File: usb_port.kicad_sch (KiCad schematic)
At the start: 14 parts, among them J1 USB_C_Receptacle, U12 MT9700

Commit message: Finish layout
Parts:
- renumbered C76 to C68, C66 to C78, C67 to C79, C69 to C81, D9 to D12, F12 to F15, FB17 to FB23, FB18 to FB24, U12 to U15

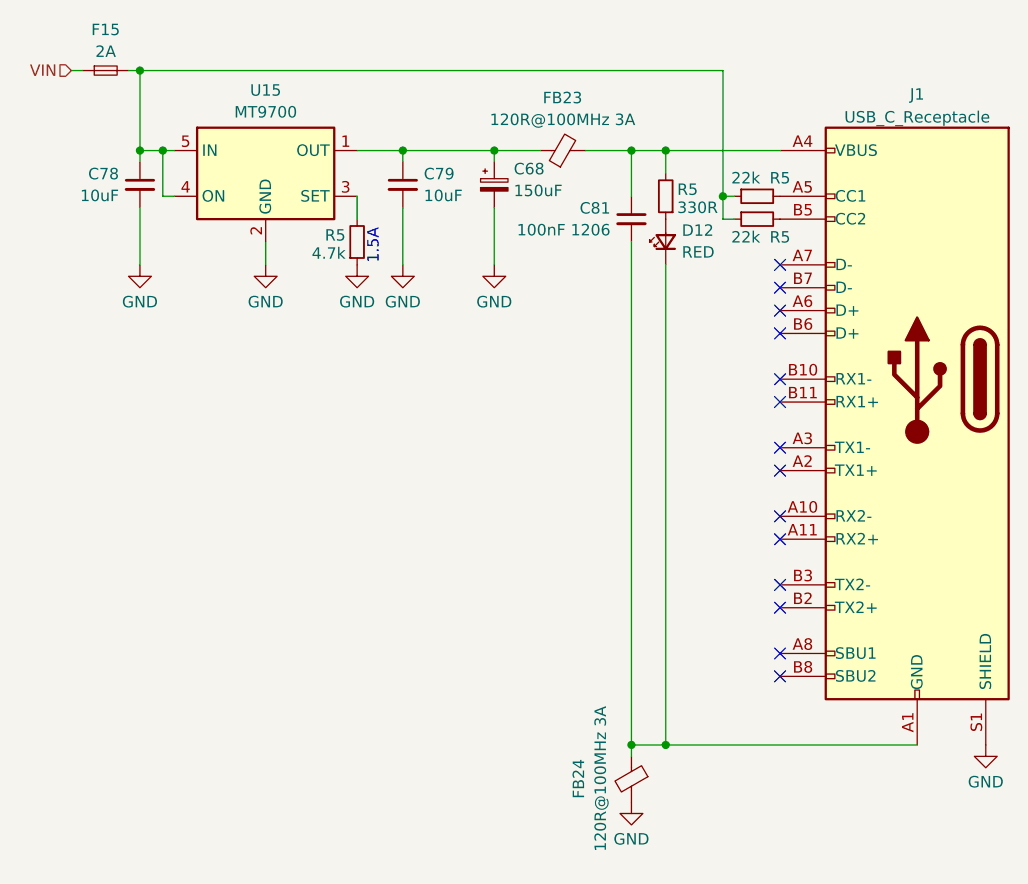
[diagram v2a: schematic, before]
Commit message: Supply regulator enable from CYPD LDO
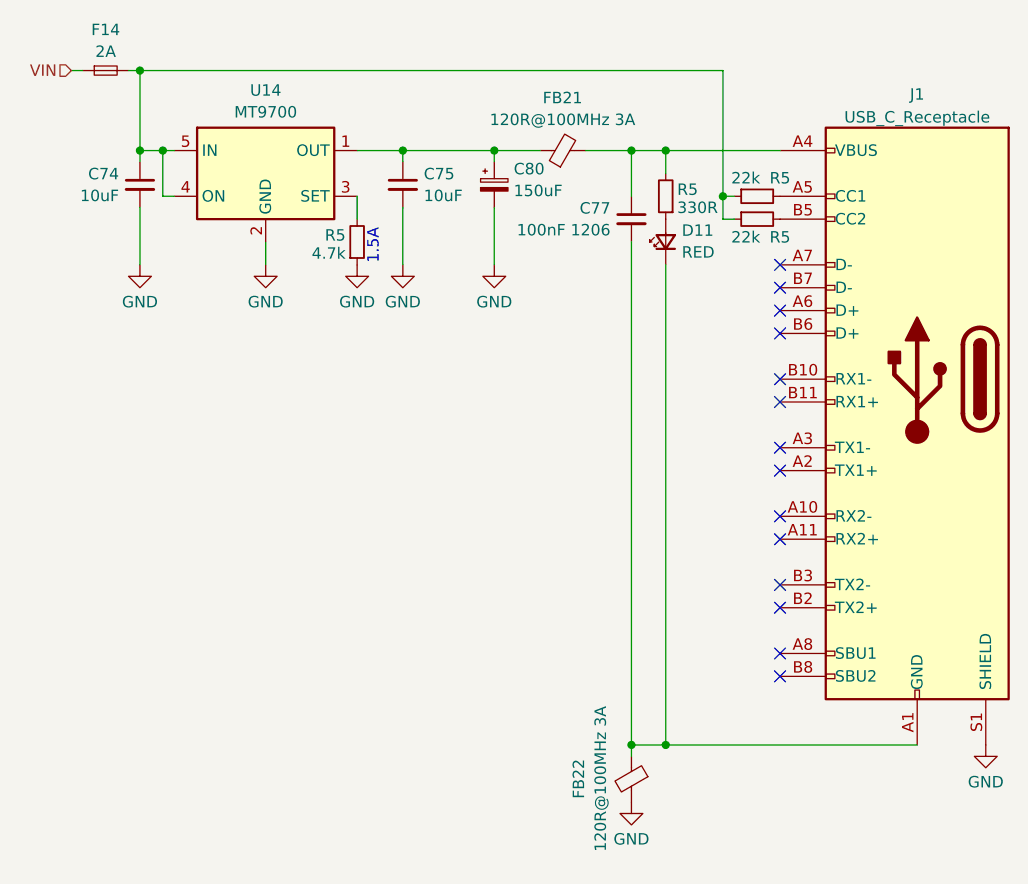
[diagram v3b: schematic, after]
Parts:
- renumbered C78 to C74, C79 to C75, C81 to C77, C68 to C80, D12 to D11, F15 to F14, FB23 to FB21, FB24 to FB22, U15 to U14

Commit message: Consolidate bom items
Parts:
- C74, C75: LCSC C15850 -> C440198

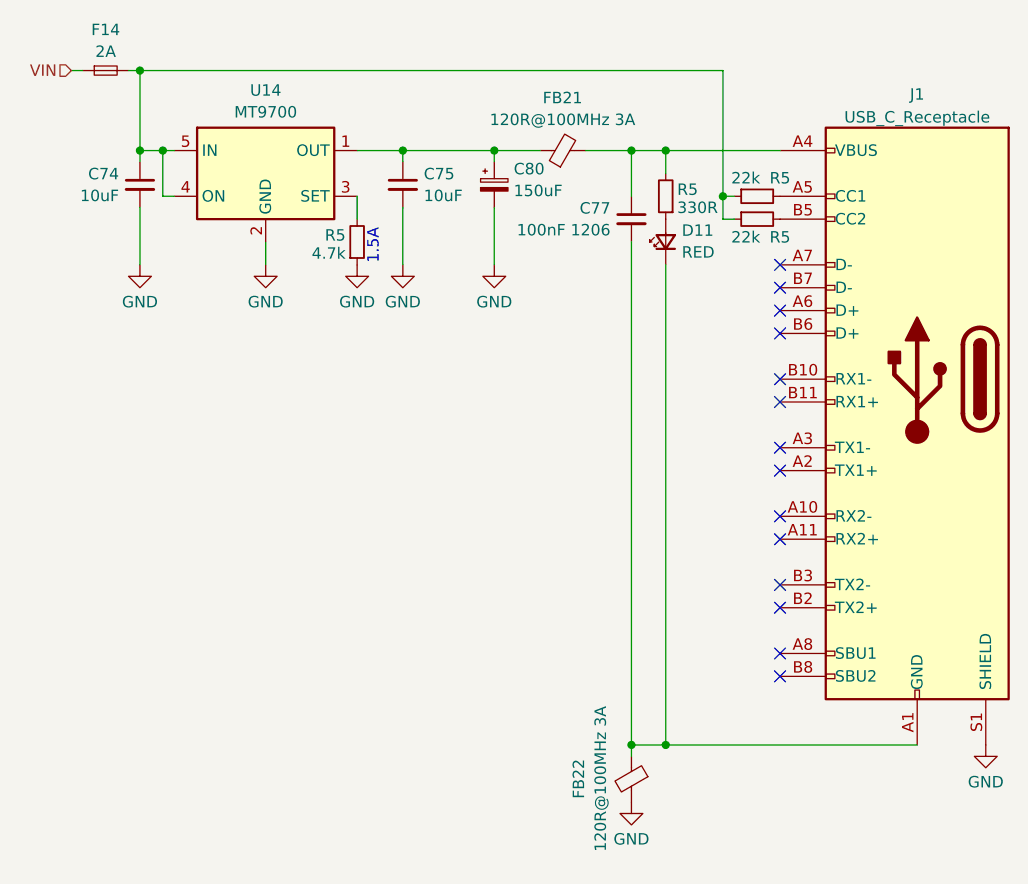
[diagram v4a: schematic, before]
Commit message: Fix LED partnumber
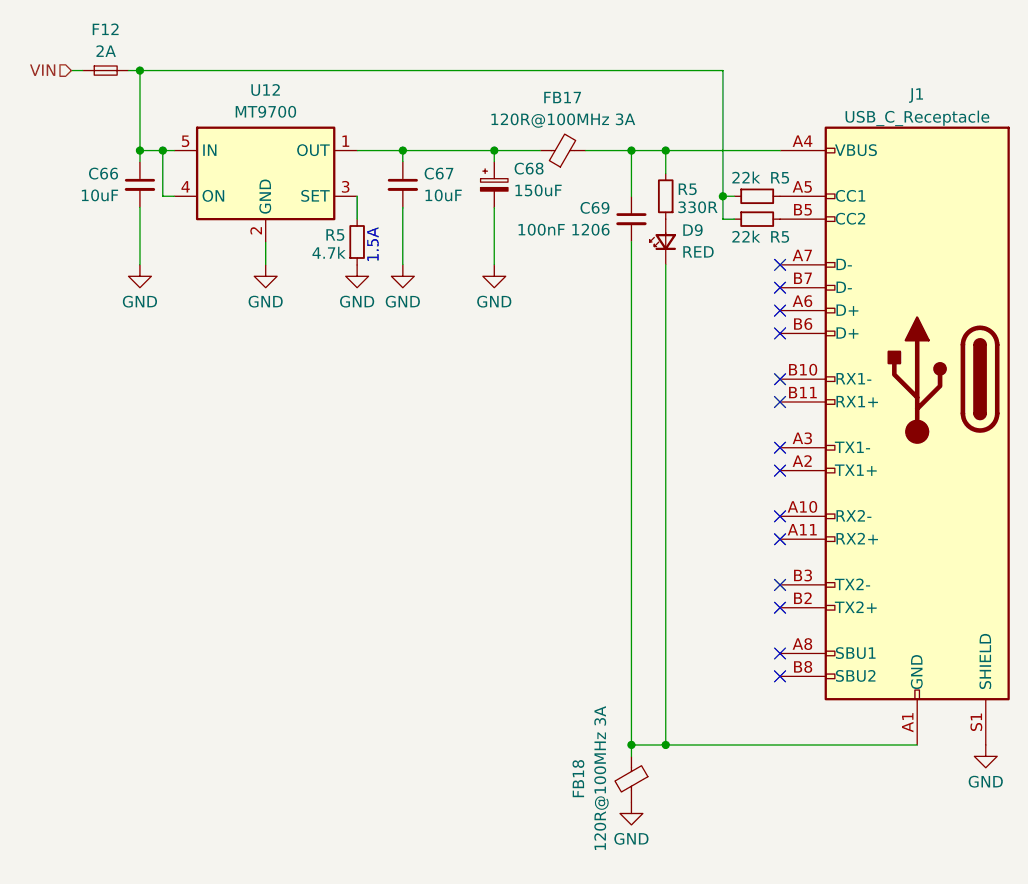
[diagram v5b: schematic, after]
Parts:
- D9: renamed from D11; LCSC C25900 -> C99771
- renumbered C74 to C66, C75 to C67, C80 to C68, C77 to C69, F14 to F12, FB21 to FB17, FB22 to FB18, U14 to U12

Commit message: Add TVS to port groups
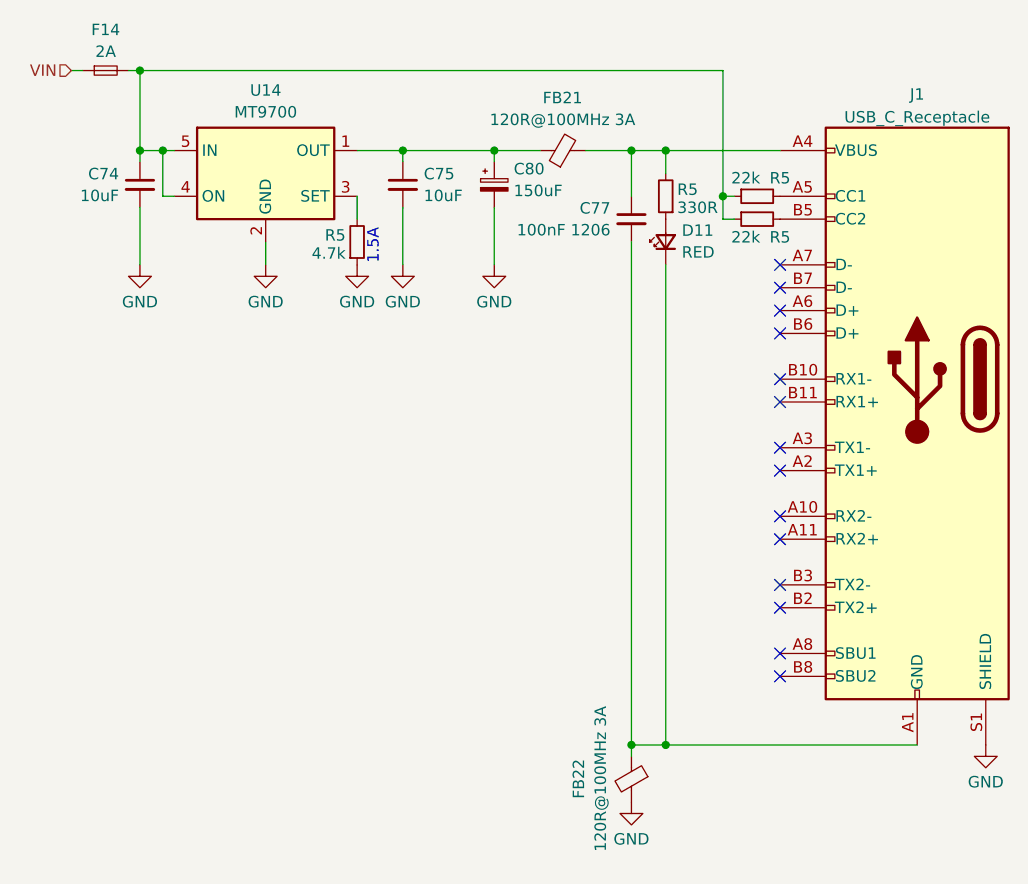
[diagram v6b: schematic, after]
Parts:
- renumbered C66 to C74, C67 to C75, C69 to C77, C68 to C80, D9 to D11, F12 to F14, FB17 to FB21, FB18 to FB22, U12 to U14

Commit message: Advertise all charging ports as DCP
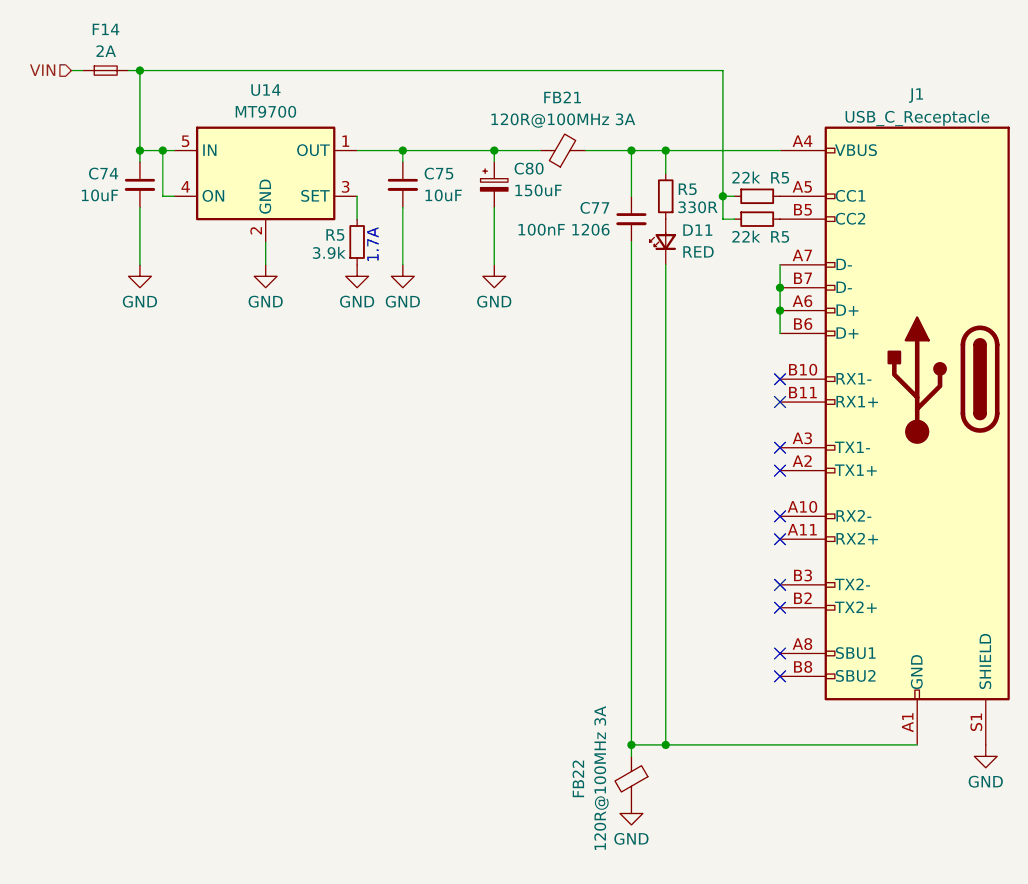
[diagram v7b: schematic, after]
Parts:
- D11: now left out of the parts list
- R5: value 4.7k -> 3.9k; LCSC C25900 -> C51721
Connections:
- net at J1.A6 (D+): now also J1.A7 (D-), J1.B6 (D+), J1.B7 (D-)
- no-connect marks 14 -> 10
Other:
- note added: "1.7A"
- note removed: "1.5A"
